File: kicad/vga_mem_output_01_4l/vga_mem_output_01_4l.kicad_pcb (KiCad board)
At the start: 4 copper layers, 80.9 x 100.6 mm, 64 parts, among them J1 Conn_01x03_Socket, J2 Conn_01x02_Socket, J3 Conn_01x08_Socket, J4 DE15_Socket_HighDensity_Mount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, J6 Conn_01x18_Socket, U1 74LS08, U10 74HCT574, U11 74HC245, U12 74AHC1GU04, U13 74LS163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

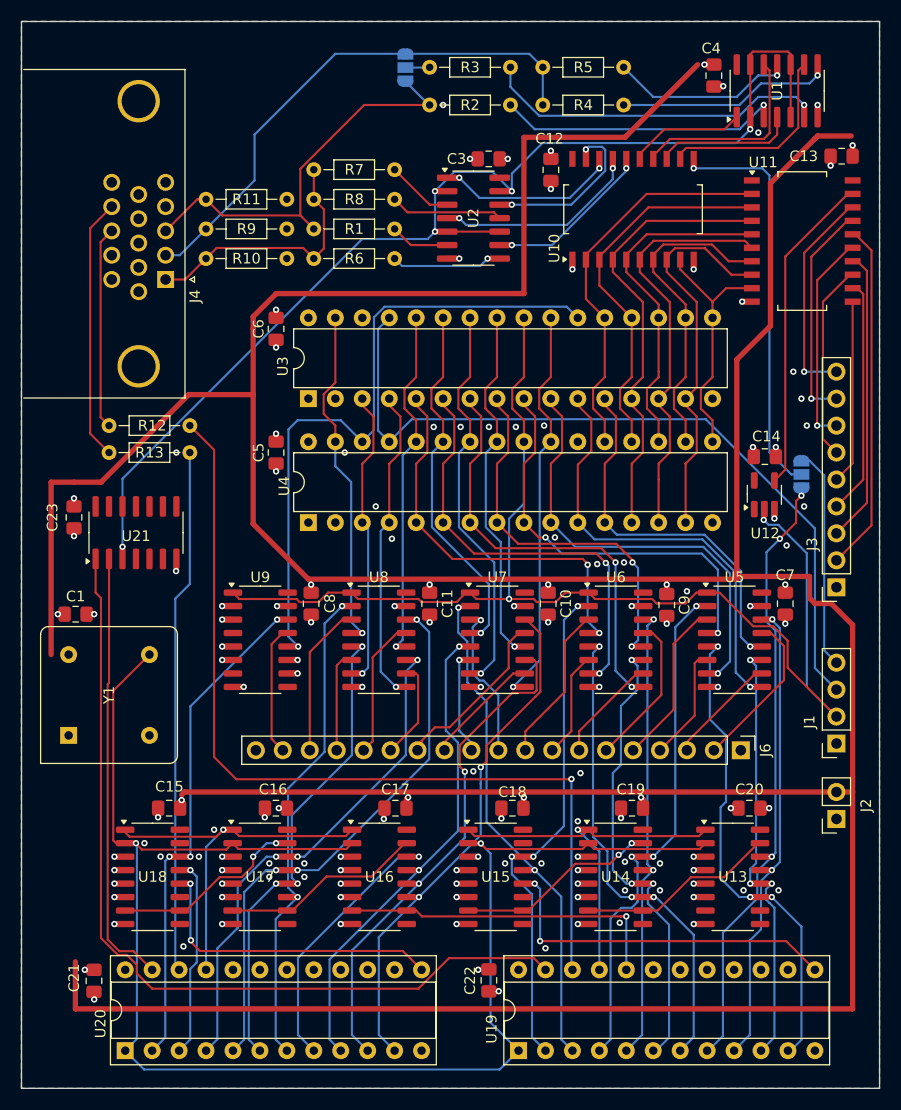
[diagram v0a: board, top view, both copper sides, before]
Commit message: changed connector positions
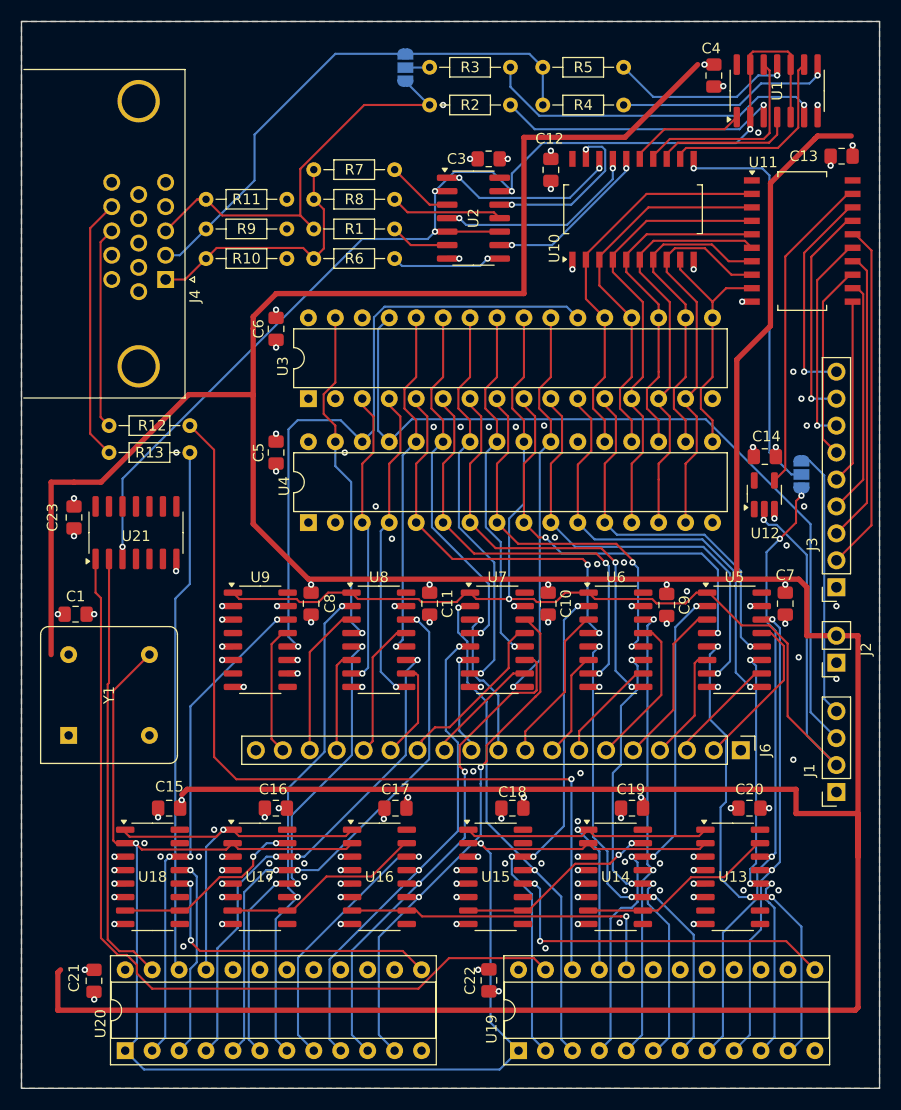
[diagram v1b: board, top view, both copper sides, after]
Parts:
- moved J2 14.7 mm to (127.0, 103.6)
- moved J1 4.57 mm to (127.0, 115.8)
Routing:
- net VCC: track 424.5 -> 434.4 mm, vias 22 -> 26
- net /~{A_FRONT}: track 117.2 -> 126.1 mm
- net /~{WE}: track 73.9 -> 78.4 mm
- net /H0_EXT: track 20.9 -> 25.4 mm
